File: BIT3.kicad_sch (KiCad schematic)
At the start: 48 parts, among them J1 Conn_02x04_Odd_Even, J2 Conn_01x02_Pin, J3 Conn_01x04_Socket, J4 Conn_02x02_Odd_Even, Q1 BSP89, SW1 SW_SPDT, SW2 SW_Push, SW3 SW_Push, U2 FODM217A, U3 FODM217A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

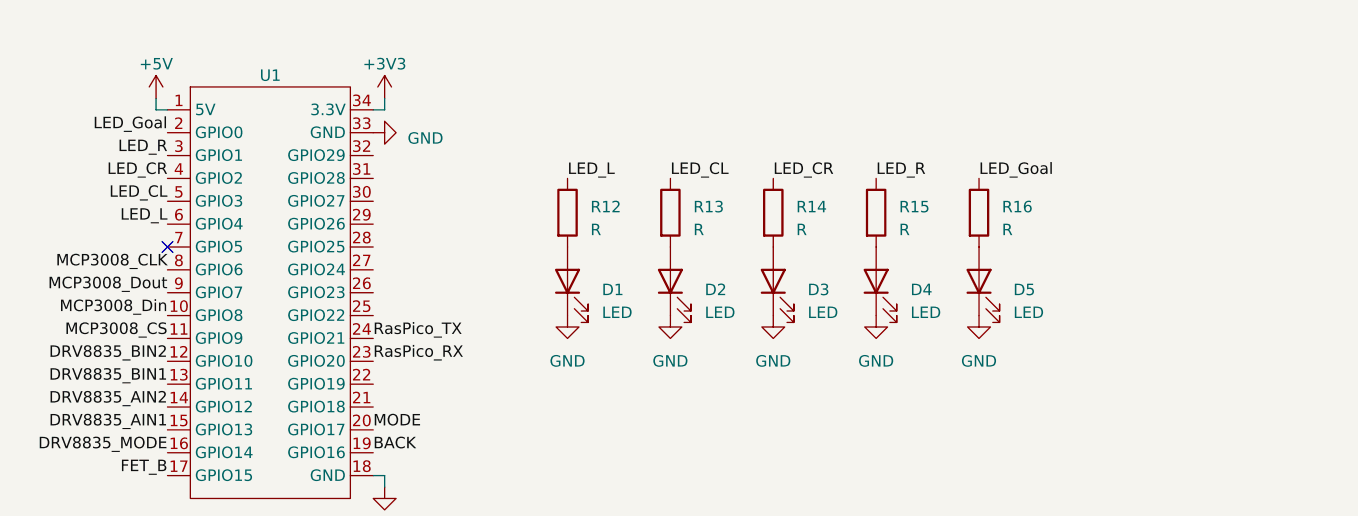
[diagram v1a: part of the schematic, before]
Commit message: 7 セグメント LED 用フットプリントを追加
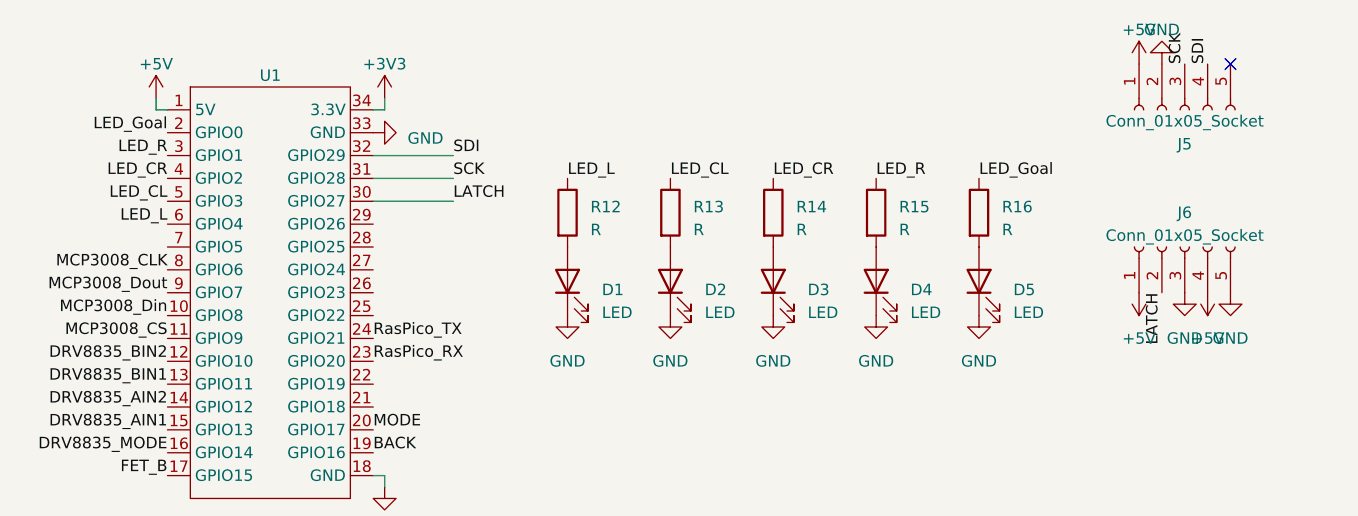
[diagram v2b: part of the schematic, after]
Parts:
- added J5, J6: Conn_01x05_Socket, Connector_PinSocket_2.54mm:PinSocket_1x05_P2.54mm_Vertical, symbol Connector:Conn_01x05_Socket
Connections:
- net +5V: now also J5.1 (Pin_1), J6.1 (Pin_1), J6.4 (Pin_4)
- net GND: now also J5.2 (Pin_2), J6.3 (Pin_3), J6.5 (Pin_5)
- net LATCH: now reaches U1.30 (GPIO27)
- net LATCH: now also J6.2 (Pin_2)
- net SCK: now reaches U1.31 (GPIO28)
- net SCK: now also J5.3 (Pin_3)
- net SDI: now reaches U1.32 (GPIO29)
- net SDI: now also J5.4 (Pin_4)
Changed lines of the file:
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@@
   (no_connect (at 198.12 119.38))
   (no_connect (at 36.83 149.86))
-  (no_connect (at 147.32 83.82))
+  (no_connect (at 265.43 63.5))
   (no_connect (at 36.83 147.32))
   (wire (pts (xy 233.68 123.19) (xy 233.68 124.46))
@@
     (stroke (width 0) (type default))
   )
+  (wire (pts (xy 170.18 78.74) (xy 179.07 78.74))
+    (stroke (width 0) (type default))
+  )
   (wire (pts (xy 130.81 177.8) (xy 130.81 176.53))
     (stroke (width 0) (type default))
@@
     (stroke (width 0) (type default))
   )
+  (wire (pts (xy 170.18 76.2) (xy 179.07 76.2))
+    (stroke (width 0) (type default))
+  )
   (wire (pts (xy 124.46 134.62) (xy 124.46 135.89))
     (stroke (width 0) (type default))
@@
     (stroke (width 0) (type default))
   )
+  (wire (pts (xy 170.18 73.66) (xy 179.07 73.66))
+    (stroke (width 0) (type default))
+  )
   (wire (pts (xy 44.45 74.93) (xy 44.45 77.47))
     (stroke (width 0) (type default))
@@
     (effects (font (size 1.27 1.27)) (justify left bottom))
   )
+  (label "SCK" (at 179.07 76.2 0) (fields_autoplaced)
+    (effects (font (size 1.27 1.27)) (justify left bottom))
+  )
   (label "RasPico_TX" (at 170.18 93.98 0) (fields_autoplaced)
     (effects (font (size 1.27 1.27)) (justify left bottom))
   )
+  (label "SDI" (at 179.07 73.66 0) (fields_autoplaced)
+    (effects (font (size 1.27 1.27)) (justify left bottom))
+  )
   (label "DRV8835_BIN2" (at 123.19 148.59 0) (fields_autoplaced)
     (effects (font (size 1.27 1.27)) (justify left bottom))
@@
     (effects (font (size 1.27 1.27)) (justify right bottom))
   )
+  (label "LATCH" (at 179.07 78.74 0) (fields_autoplaced)
+    (effects (font (size 1.27 1.27)) (justify left bottom))
+  )
   (label "RasPico_RX" (at 170.18 96.52 0) (fields_autoplaced)
     (effects (font (size 1.27 1.27)) (justify left bottom))
@@
     (effects (font (size 1.27 1.27)) (justify right bottom))
   )
+  (label "SCK" (at 260.35 63.5 90) (fields_autoplaced)
+    (effects (font (size 1.27 1.27)) (justify left bottom))
+  )
   (label "LED_Goal" (at 237.49 76.2 0) (fields_autoplaced)
     (effects (font (size 1.27 1.27)) (justify left bottom))
@@
   )
   (label "LED_R" (at 147.32 73.66 180) (fields_autoplaced)
+    (effects (font (size 1.27 1.27)) (justify right bottom))
+  )
+  (label "SDI" (at 262.89 63.5 90) (fields_autoplaced)
+    (effects (font (size 1.27 1.27)) (justify left bottom))
+  )
+  (label "LATCH" (at 257.81 88.9 270) (fields_autoplaced)
     (effects (font (size 1.27 1.27)) (justify right bottom))
   )
@@
         (path "/e911d5a5-765c-4e39-aa6a-9a13739432fd"
           (reference "U4") (unit 1)
+        )
+      )
+    )
+  )
+  (symbol (lib_id "Connector:Conn_01x05_Socket") (at 260.35 83.82 90) (unit 1)
+    (in_bom yes) (on_board yes) (dnp no)
+    (property "Reference" "J6" (at 260.35 80.01 90)
+      (effects (font (size 1.27 1.27)))
+    )
+    (property "Value" "Conn_01x05_Socket" (at 260.35 82.55 90)
+      (effects (font (size 1.27 1.27)))
+    )
+    (property "Footprint" "Connector_PinSocket_2.54mm:PinSocket_1x05_P2.54mm_Vertical" (at 260.35 83.82 0)
+      (effects (font (size 1.27 1.27)) hide)
+    )
+    (property "Datasheet" "~" (at 260.35 83.82 0)
+      (effects (font (size 1.27 1.27)) hide)
+    )
+    (pin "1")
+    (pin "2")
+    (pin "3")
+    (pin "4")
+    (pin "5")
+    (instances
+      (project "BIT3"
+        (path "/e911d5a5-765c-4e39-aa6a-9a13739432fd"
+          (reference "J6") (unit 1)
         )
       )
@@
     )
   )
+  (symbol (lib_id "power:+5V") (at 255.27 63.5 0) (unit 1)
+    (in_bom yes) (on_board yes) (dnp no) (fields_autoplaced)
+    (property "Reference" "#PWR029" (at 255.27 67.31 0)
+      (effects (font (size 1.27 1.27)) hide)
+    )
+    (property "Value" "+5V" (at 255.27 59.69 0)
+      (effects (font (size 1.27 1.27)))
+    )
+    (property "Footprint" "" (at 255.27 63.5 0)
+      (effects (font (size 1.27 1.27)) hide)
+    )
+    (property "Datasheet" "" (at 255.27 63.5 0)
+      (effects (font (size 1.27 1.27)) hide)
+    )
+    (pin "1")
+    (instances
+      (project "BIT3"
+        (path "/e911d5a5-765c-4e39-aa6a-9a13739432fd"
+          (reference "#PWR029") (unit 1)
+        )
+      )
+    )
+  )
   (symbol (lib_id "power:GND") (at 57.15 157.48 0) (unit 1)
     (in_bom yes) (on_board yes) (dnp no) (fields_autoplaced)
@@
         (path "/e911d5a5-765c-4e39-aa6a-9a13739432fd"
           (reference "U3") (unit 1)
+        )
+      )
+    )
+  )
+  (symbol (lib_id "power:+5V") (at 255.27 88.9 180) (unit 1)
+    (in_bom yes) (on_board yes) (dnp no) (fields_autoplaced)
+    (property "Reference" "#PWR033" (at 255.27 85.09 0)
+      (effects (font (size 1.27 1.27)) hide)
+    )
+    (property "Value" "+5V" (at 255.27 93.98 0)
+      (effects (font (size 1.27 1.27)))
+    )
+    (property "Footprint" "" (at 255.27 88.9 0)
+      (effects (font (size 1.27 1.27)) hide)
+    )
+    (property "Datasheet" "" (at 255.27 88.9 0)
+      (effects (font (size 1.27 1.27)) hide)
+    )
+    (pin "1")
+    (instances
+      (project "BIT3"
+        (path "/e911d5a5-765c-4e39-aa6a-9a13739432fd"
+          (reference "#PWR033") (unit 1)
         )
       )
@@
     )
   )
+  (symbol (lib_id "power:+5V") (at 262.89 88.9 180) (unit 1)
+    (in_bom yes) (on_board yes) (dnp no) (fields_autoplaced)
+    (property "Reference" "#PWR031" (at 262.89 85.09 0)
+      (effects (font (size 1.27 1.27)) hide)
+    )
+    (property "Value" "+5V" (at 262.89 93.98 0)
+      (effects (font (size 1.27 1.27)))
+    )
+    (property "Footprint" "" (at 262.89 88.9 0)
+      (effects (font (size 1.27 1.27)) hide)
+    )
+    (property "Datasheet" "" (at 262.89 88.9 0)
+      (effects (font (size 1.27 1.27)) hide)
+    )
+    (pin "1")
+    (instances
+      (project "BIT3"
+        (path "/e911d5a5-765c-4e39-aa6a-9a13739432fd"
+          (reference "#PWR031") (unit 1)
+        )
+      )
+    )
+  )
   (symbol (lib_id "Device:R") (at 29.21 71.12 0) (unit 1)
     (in_bom yes) (on_board yes) (dnp no) (fields_autoplaced)
@@
     )
   )
+  (symbol (lib_id "power:GND") (at 265.43 88.9 0) (unit 1)
+    (in_bom yes) (on_board yes) (dnp no) (fields_autoplaced)
+    (property "Reference" "#PWR030" (at 265.43 95.25 0)
+      (effects (font (size 1.27 1.27)) hide)
+    )
+    (property "Value" "GND" (at 265.43 93.98 0)
+      (effects (font (size 1.27 1.27)))
+    )
+    (property "Footprint" "" (at 265.43 88.9 0)
+      (effects (font (size 1.27 1.27)) hide)
+    )
+    (property "Datasheet" "" (at 265.43 88.9 0)
+      (effects (font (size 1.27 1.27)) hide)
+    )
+    (pin "1")
+    (instances
+      (project "BIT3"
+        (path "/e911d5a5-765c-4e39-aa6a-9a13739432fd"
+          (reference "#PWR030") (unit 1)
+        )
+      )
+    )
+  )
+  (symbol (lib_id "Connector:Conn_01x05_Socket") (at 260.35 68.58 90) (mirror x) (unit 1)
+    (in_bom yes) (on_board yes) (dnp no) (fields_autoplaced)
+    (property "Reference" "J5" (at 260.35 72.39 90)
+      (effects (font (size 1.27 1.27)))
+    )
+    (property "Value" "Conn_01x05_Socket" (at 260.35 69.85 90)
+      (effects (font (size 1.27 1.27)))
+    )
+    (property "Footprint" "Connector_PinSocket_2.54mm:PinSocket_1x05_P2.54mm_Vertical" (at 260.35 68.58 0)
+      (effects (font (size 1.27 1.27)) hide)
+    )
+    (property "Datasheet" "~" (at 260.35 68.58 0)
+      (effects (font (size 1.27 1.27)) hide)
+    )
+    (pin "1")
+    (pin "2")
+    (pin "3")
+    (pin "4")
+    (pin "5")
+    (instances
+      (project "BIT3"
+        (path "/e911d5a5-765c-4e39-aa6a-9a13739432fd"
+          (reference "J5") (unit 1)
+        )
+      )
+    )
+  )
   (symbol (lib_id "power:+5V") (at 233.68 123.19 0) (unit 1)
     (in_bom yes) (on_board yes) (dnp no) (fields_autoplaced)
@@
         (path "/e911d5a5-765c-4e39-aa6a-9a13739432fd"
           (reference "#PWR021") (unit 1)
+        )
+      )
+    )
+  )
+  (symbol (lib_id "power:GND") (at 260.35 88.9 0) (unit 1)
+    (in_bom yes) (on_board yes) (dnp no) (fields_autoplaced)
+    (property "Reference" "#PWR032" (at 260.35 95.25 0)
+      (effects (font (size 1.27 1.27)) hide)
+    )
+    (property "Value" "GND" (at 260.35 93.98 0)
+      (effects (font (size 1.27 1.27)))
+    )
+    (property "Footprint" "" (at 260.35 88.9 0)
+      (effects (font (size 1.27 1.27)) hide)
+    )
+    (property "Datasheet" "" (at 260.35 88.9 0)
+      (effects (font (size 1.27 1.27)) hide)
+    )
+    (pin "1")
+    (instances
+      (project "BIT3"
+        (path "/e911d5a5-765c-4e39-aa6a-9a13739432fd"
+          (reference "#PWR032") (unit 1)
         )
       )
@@
         )
       )
+    )
+  )
+  (symbol (lib_id "power:GND") (at 257.81 63.5 180) (unit 1)
+    (in_bom yes) (on_board yes) (dnp no) (fields_autoplaced)
+    (property "Reference" "#PWR028" (at 257.81 57.15 0)
+      (effects (font (size 1.27 1.27)) hide)
+    )
+    (property "Value" "GND" (at 257.81 59.69 0)
+      (effects (font (size 1.27 1.27)))
+    )
+    (property "Footprint" "" (at 257.81 63.5 0)
+      (effects (font (size 1.27 1.27)) hide)
+    )
+    (property "Datasheet" "" (at 257.81 63.5 0)
+      (effects (font (size 1.27 1.27)) hide)
+    )
+    (pin "1")
+    (instances
+      (project "BIT3"
+        (path "/e911d5a5-765c-4e39-aa6a-9a13739432fd"
+          (reference "#PWR028") (unit 1)
+        )
+      )
